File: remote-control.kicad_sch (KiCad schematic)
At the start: 17 parts, among them J1 USB_B_Micro, J2 Conn_01x08_Pin, U1 ESP32S3WROOM1N8R8, U2 ESD321DPYR, U3 ESD321DPYR, U4 CP2102N-Axx-xQFN28, U5 BQ24079RGT, U6 AMS1117-3.3

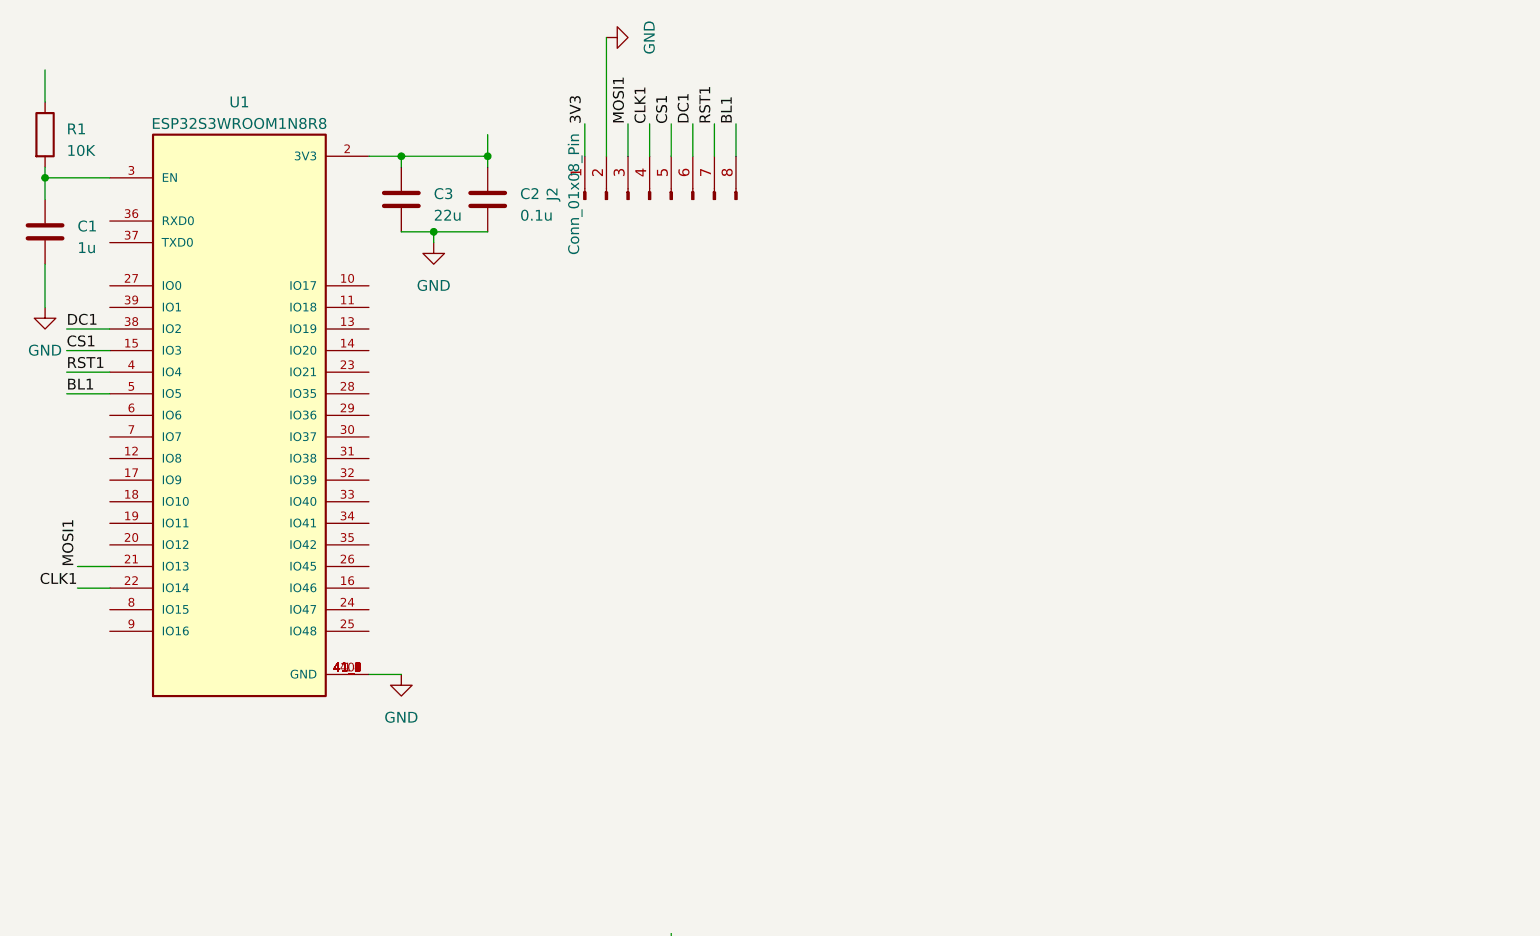
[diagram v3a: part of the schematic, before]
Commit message: add buttons and joytic to schematic
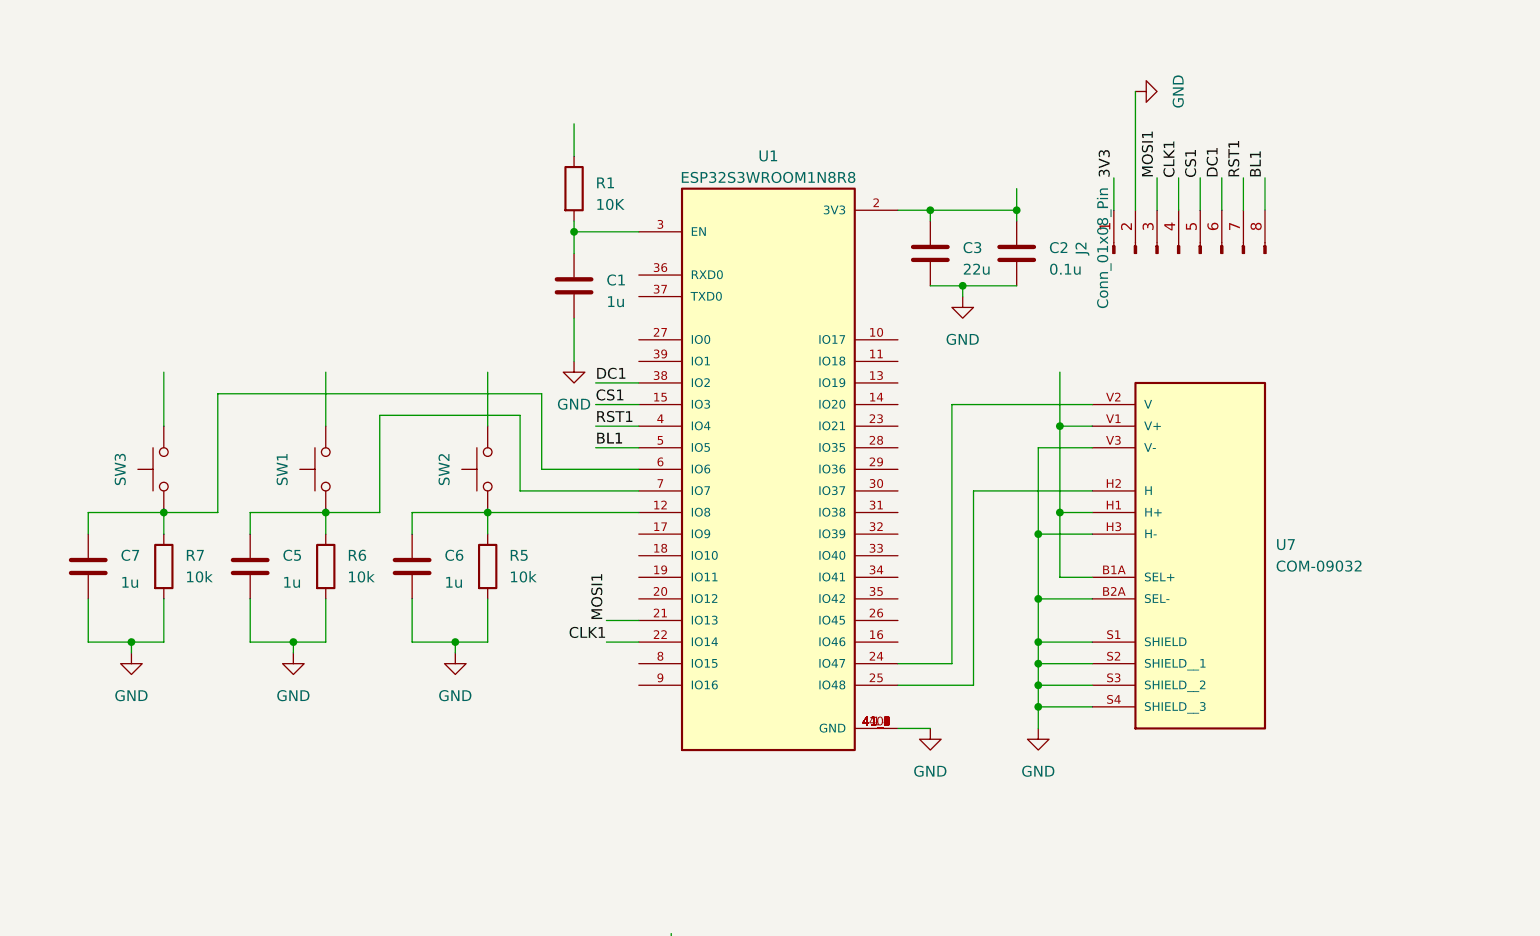
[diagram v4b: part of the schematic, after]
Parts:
- added C5, C6, C7: 1u, symbol Device:C
- added R5, R6, R7: 10k, symbol Device:R
- added SW1, SW2, SW3: SW_MEC_5G, Button_Switch_SMD:SW_MEC_5GSH9, symbol Switch:SW_MEC_5G
- added U7: COM-09032, COM-09032:XDCR_COM-09032, symbol COM-09032:COM-09032
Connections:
- net GND: now also C5.2, C6.2, C7.2, R5.2, R6.2, R7.2, U7.B2A (SEL-), U7.H3 (H-), U7.S1 (SHIELD), U7.S2 (SHIELD__1), U7.S3 (SHIELD__2), U7.S4 (SHIELD__3), U7.V3 (V-)
- net at U1.12 (IO8): now also C6.1, R5.1, SW2.1 (A), SW2.2 (A)
- net at U1.24 (IO47): now also U7.V2 (V)
- net at U1.25 (IO48): now also U7.H2 (H)
- net at U1.6 (IO6): now also C7.1, R7.1, SW3.1 (A), SW3.2 (A)
- net at U1.7 (IO7): now also C5.1, R6.1, SW1.1 (A), SW1.2 (A)
- new net: SW1.3 (B), SW1.4 (B)
- new net: SW3.3 (B), SW3.4 (B)
- new net: SW2.3 (B), SW2.4 (B)
- new net: U7.B1A (SEL+), U7.H1 (H+), U7.V1 (V+)
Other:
- moved on the sheet: C1, C2, C3, J2, R1, U1

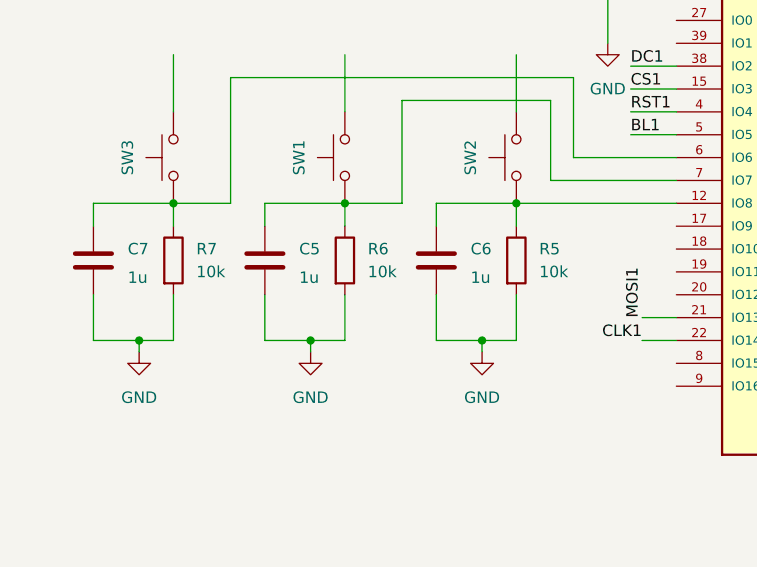
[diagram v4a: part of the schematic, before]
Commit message: update resistor and capacitor values
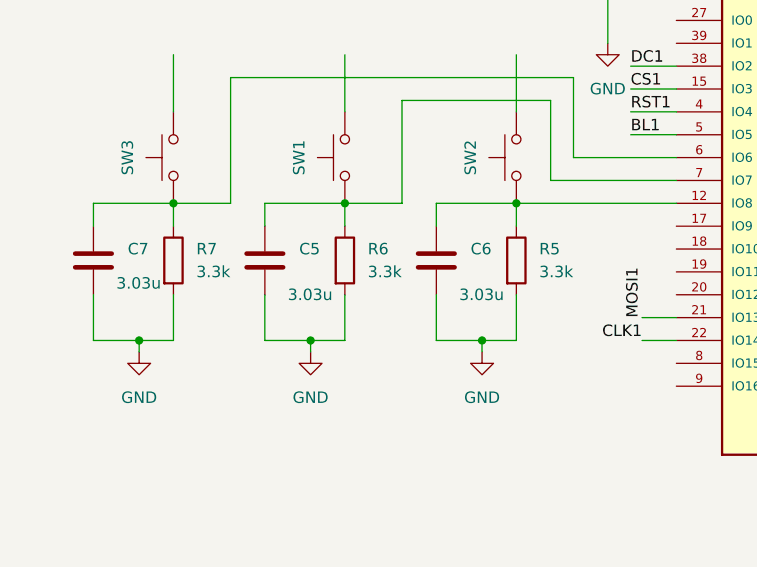
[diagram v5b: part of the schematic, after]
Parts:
- C5, C6, C7: value 1u -> 3.03u
- R5, R6, R7: value 10k -> 3.3k
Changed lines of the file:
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@@
       (effects (font (size 1.27 1.27)) (justify left))
     )
-    (property "Value" "10k" (at 36.83 78.74 0)
+    (property "Value" "3.3k" (at 36.83 78.74 0)
       (effects (font (size 1.27 1.27)) (justify left))
     )
@@
       (effects (font (size 1.27 1.27)) (justify left))
     )
-    (property "Value" "1u" (at 29.21 79.375 0)
+    (property "Value" "3.03u" (at 27.94 80.01 0)
       (effects (font (size 1.27 1.27)) (justify left))
     )
@@
       (effects (font (size 1.27 1.27)) (justify left))
     )
-    (property "Value" "1u" (at 48.26 79.375 0)
+    (property "Value" "3.03u" (at 46.99 81.28 0)
       (effects (font (size 1.27 1.27)) (justify left))
     )
@@
       (effects (font (size 1.27 1.27)) (justify left))
     )
-    (property "Value" "1u" (at 67.31 79.375 0)
+    (property "Value" "3.03u" (at 66.04 81.28 0)
       (effects (font (size 1.27 1.27)) (justify left))
     )
@@
       (effects (font (size 1.27 1.27)) (justify left))
     )
-    (property "Value" "10k" (at 74.93 78.74 0)
+    (property "Value" "3.3k" (at 74.93 78.74 0)
       (effects (font (size 1.27 1.27)) (justify left))
     )
@@
       (effects (font (size 1.27 1.27)) (justify left))
     )
-    (property "Value" "10k" (at 55.88 78.74 0)
-      (effects (font (size 1.27 1.27)) (justify left))
-    )
+    (property "Value" "3.3k" (at 55.88 78.74 0)
+      (effects (font (size 1.27 1.27)) (justify left))
+    )

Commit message: Add joystick terminal
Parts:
- added J3: Micro_SD_Card, symbol Connector:Micro_SD_Card
- added J4: Conn_01x05_Pin, symbol Connector:Conn_01x05_Pin
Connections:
- net GND: now also J3.6 (VSS), J4.1 (Pin_1)
- net CS2: now reaches U1.10 (IO17)
- net CS2: now also J3.2 (DAT3/CD)
- net MOSI2: now reaches U1.11 (IO18)
- net MOSI2: now also J3.3 (CMD)
- net CLK2: now reaches U1.13 (IO19)
- net CLK2: now also J3.5 (CLK)
- net MISO2: now reaches U1.14 (IO20)
- net MISO2: now also J3.7 (DAT0)
- net JOYX: now reaches U1.23 (IO21)
- net JOYX: now also J4.3 (Pin_3)
- net JOYY: now reaches U1.28 (IO35)
- net JOYY: now also J4.4 (Pin_4)
- net JOYSW: now reaches U1.29 (IO36)
- net JOYSW: now also J4.5 (Pin_5)
- no-connect marks 1 -> 3
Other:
- note added: "Display terminal"
- note added: "Joystick terminal"
- moved on the sheet: J2, R2, R3
